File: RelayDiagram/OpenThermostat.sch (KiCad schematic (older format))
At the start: 18 parts, among them J2 Conn_01x15_Female, J3 Conn_01x15_Female

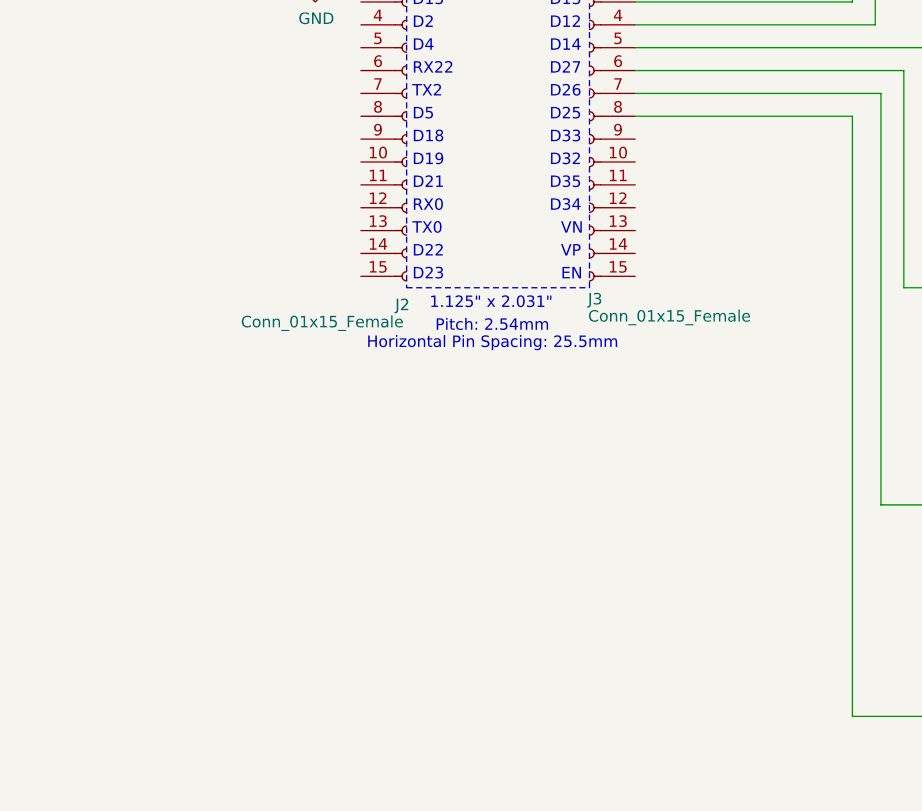
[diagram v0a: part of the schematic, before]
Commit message: Added LCD to full schematic, Changed LCD Symbol
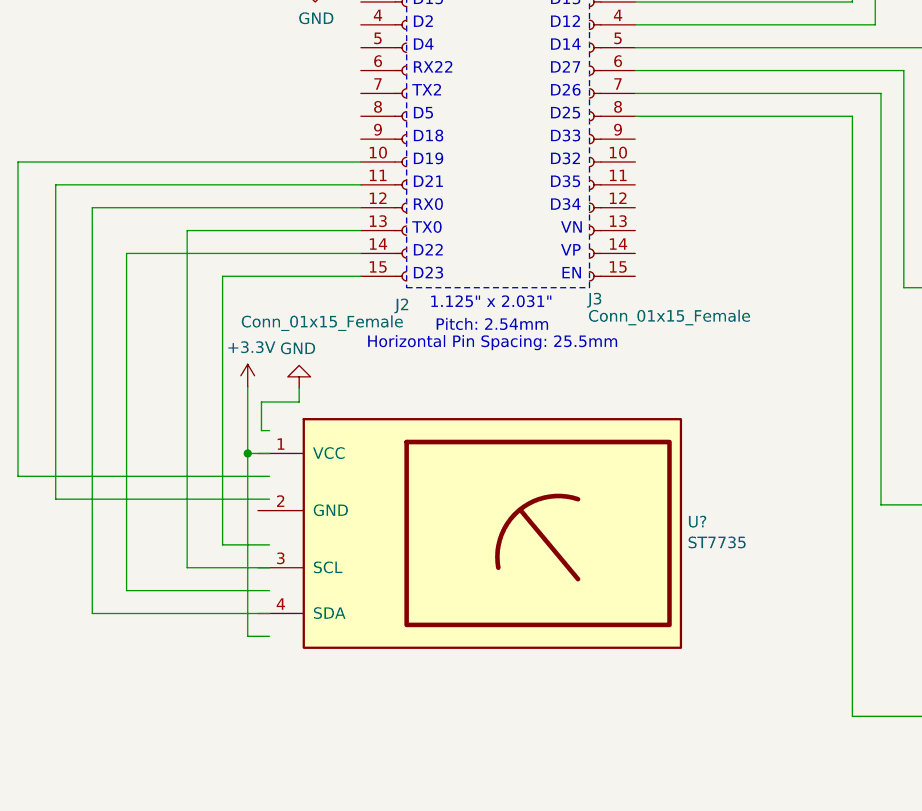
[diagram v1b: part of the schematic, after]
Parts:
- added U?: ST7735, symbol SeniorDesignLibrary:ST7735
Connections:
- net labels added: +3.3V
- wire segments 109 -> 135
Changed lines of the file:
@@
 Wire Wire Line
 	7700 1425 7750 1425
+$Comp
+L SeniorDesignLibrary:ST7735 U?
+U 1 1 5C414B96
+P 2900 5200
+F 0 "U?" H 4179 5200 50  0000 L CNN
+F 1 "ST7735" H 4179 5109 50  0000 L CNN
+F 2 "" H 2900 5200 50  0001 C CNN
+F 3 "" H 2900 5200 50  0001 C CNN
+	1    2900 5200
+	1    0    0    -1
+$EndComp
+Wire Wire Line
+	2750 4025 1725 4025
+Wire Wire Line
+	1725 4025 1725 5500
+Wire Wire Line
+	1725 5500 2350 5500
+Wire Wire Line
+	2350 5400 1990 5400
+Wire Wire Line
+	1990 5400 1990 3925
+Wire Wire Line
+	1990 3925 2750 3925
+Wire Wire Line
+	2350 5600 1575 5600
+Wire Wire Line
+	1575 5600 1575 3825
+Wire Wire Line
+	1575 3825 2750 3825
+Wire Wire Line
+	2350 5300 2145 5300
+Wire Wire Line
+	2145 5300 2145 4125
+Wire Wire Line
+	2145 4125 2750 4125
+$Comp
+L power:+3.3V #PWR?
+U 1 1 5C424F6C
+P 2255 4610
+F 0 "#PWR?" H 2255 4460 50  0001 C CNN
+F 1 "+3.3V" H 2270 4783 50  0000 C CNN
+F 2 "" H 2255 4610 50  0001 C CNN
+F 3 "" H 2255 4610 50  0001 C CNN
+	1    2255 4610
+	1    0    0    -1
+$EndComp
+$Comp
+L power:GND #PWR?
+U 1 1 5C42501F
+P 2480 4615
+F 0 "#PWR?" H 2480 4365 50  0001 C CNN
+F 1 "GND" H 2485 4442 50  0000 C CNN
+F 2 "" H 2480 4615 50  0001 C CNN
+F 3 "" H 2480 4615 50  0001 C CNN
+	1    2480 4615
+	-1   0    0    1
+$EndComp
+Wire Wire Line
+	2480 4675 2480 4615
+Wire Wire Line
+	2350 4900 2255 4900
+Wire Wire Line
+	2255 4900 2255 4610
+Wire Wire Line
+	2350 4800 2315 4800
+Wire Wire Line
+	2315 4800 2315 4675
+Wire Wire Line
+	2315 4675 2480 4675
+Wire Wire Line
+	2255 5700 2255 4900
+Wire Wire Line
+	2255 5700 2350 5700
+Connection ~ 2255 4900
+Wire Wire Line
+	2350 5100 1415 5100
+Wire Wire Line
+	1415 5100 1415 3725
+Wire Wire Line
+	1415 3725 2750 3725
+Wire Wire Line
+	2350 5000 1250 5000
+Wire Wire Line
+	1250 5000 1250 3625
+Wire Wire Line
+	1250 3625 2750 3625
 $EndSCHEMATC

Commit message: Some updates to the relay system for flyback and pulldown for FETs
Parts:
- added D? (x6): D, symbol Device:D
- added R? (x6): 100, symbol Device:R
- added R? (x6): 10k, symbol Device:R
- U?: symbol SeniorDesignLibrary:ST7735 -> OpenThermostat-rescue:ST7735-SeniorDesignLibrary
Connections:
- wire segments 135 -> 153

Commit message: added io for buttons and header for open pins, IO expander may not be needed because we have six open pins
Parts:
- removed D? (x6): D, symbol Device:D
- removed R? (x6): 100, symbol Device:R
- removed R? (x6): 10k, symbol Device:R
- added J?: Conn_01x06_Female, symbol Connector:Conn_01x06_Female
- added SW? (x6): SW_Push, symbol Switch:SW_Push
- U?: symbol OpenThermostat-rescue:ST7735-SeniorDesignLibrary -> SeniorDesignLibrary:ST7735
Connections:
- wire segments 153 -> 165

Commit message: added io expander, may need different pin for scl
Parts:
- removed J?: Conn_01x06_Female, symbol Connector:Conn_01x06_Female
- added J?: Conn_01x12_Female, symbol Connector:Conn_01x12_Female
- added R? (x3): 10k, symbol Device:R
- added U?: PCF8574, symbol Interface_Expansion:PCF8574
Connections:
- wire segments 165 -> 227

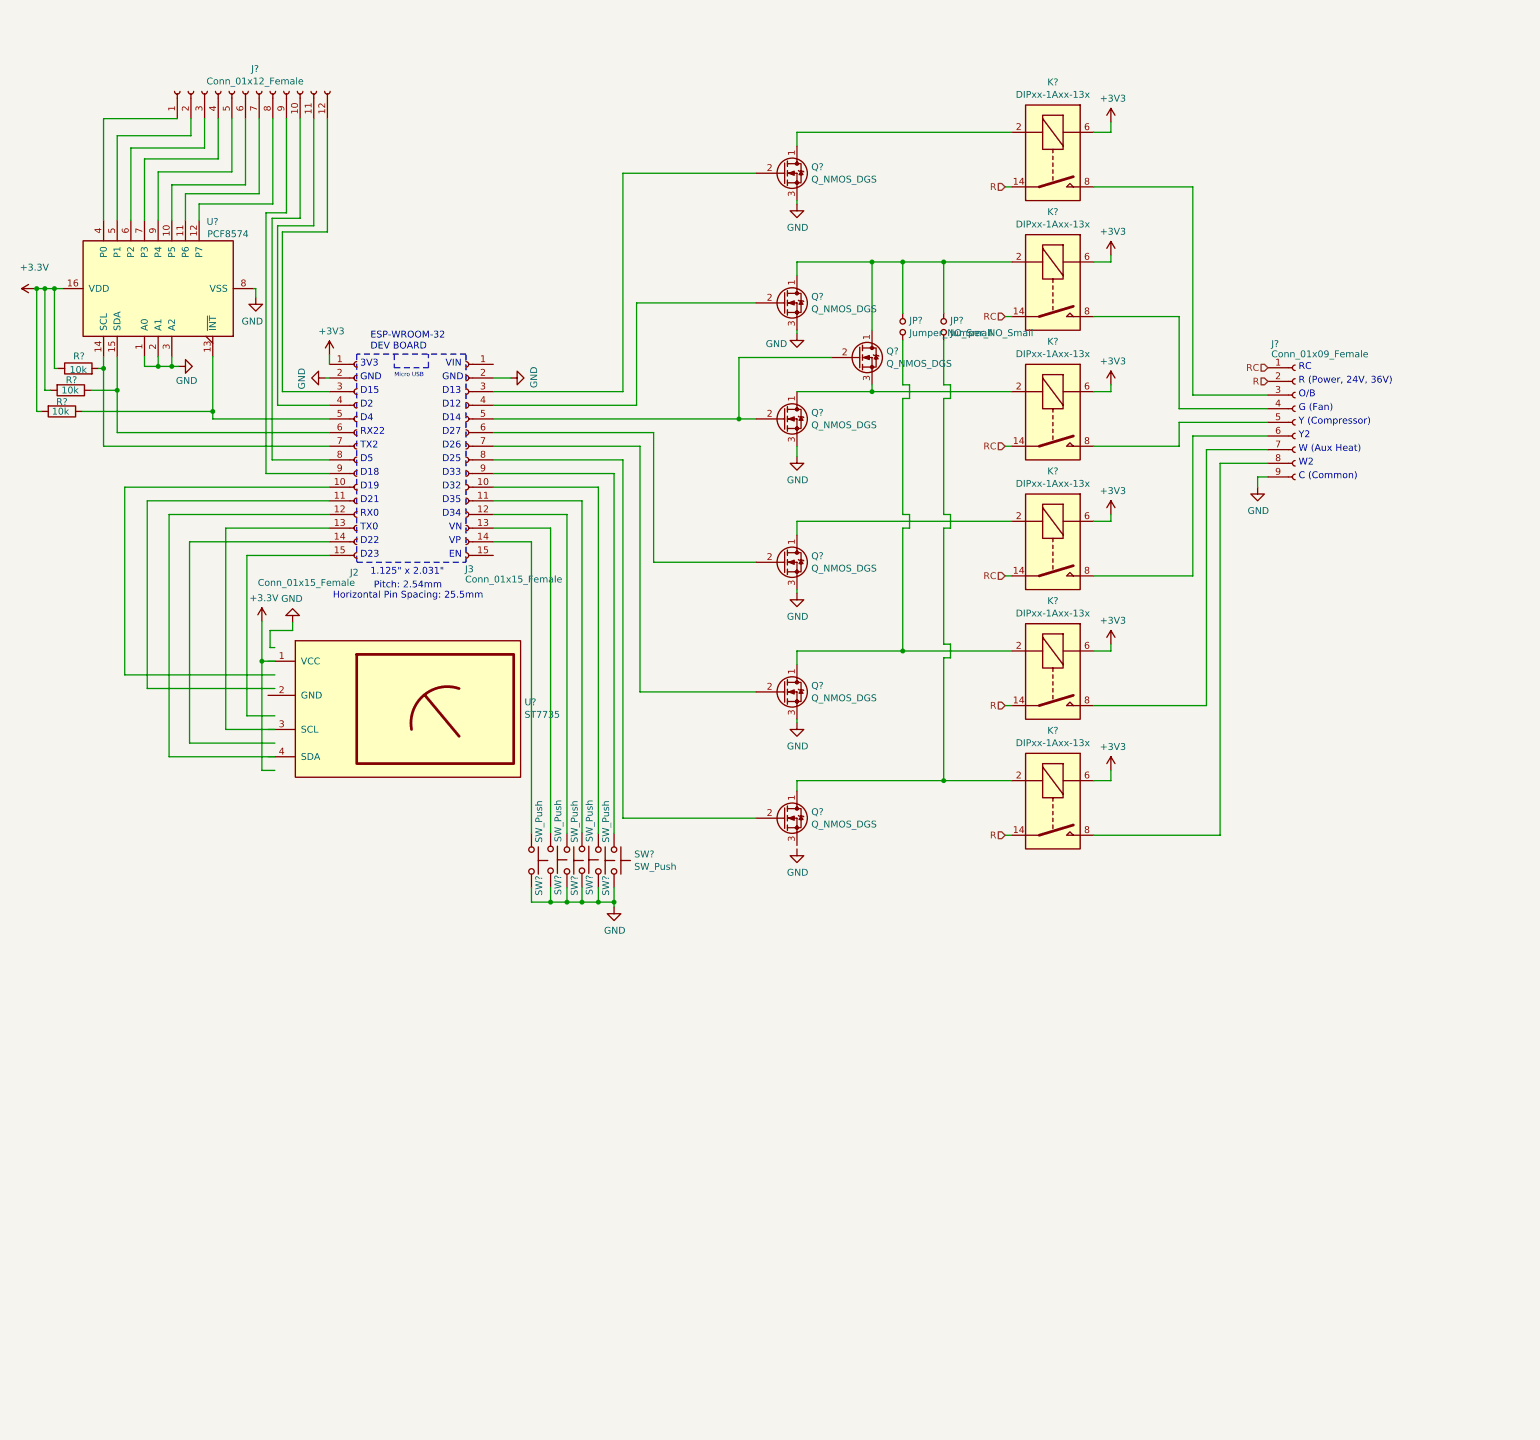
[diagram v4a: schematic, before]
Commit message: Fixed My mistake overwriting the relay protection
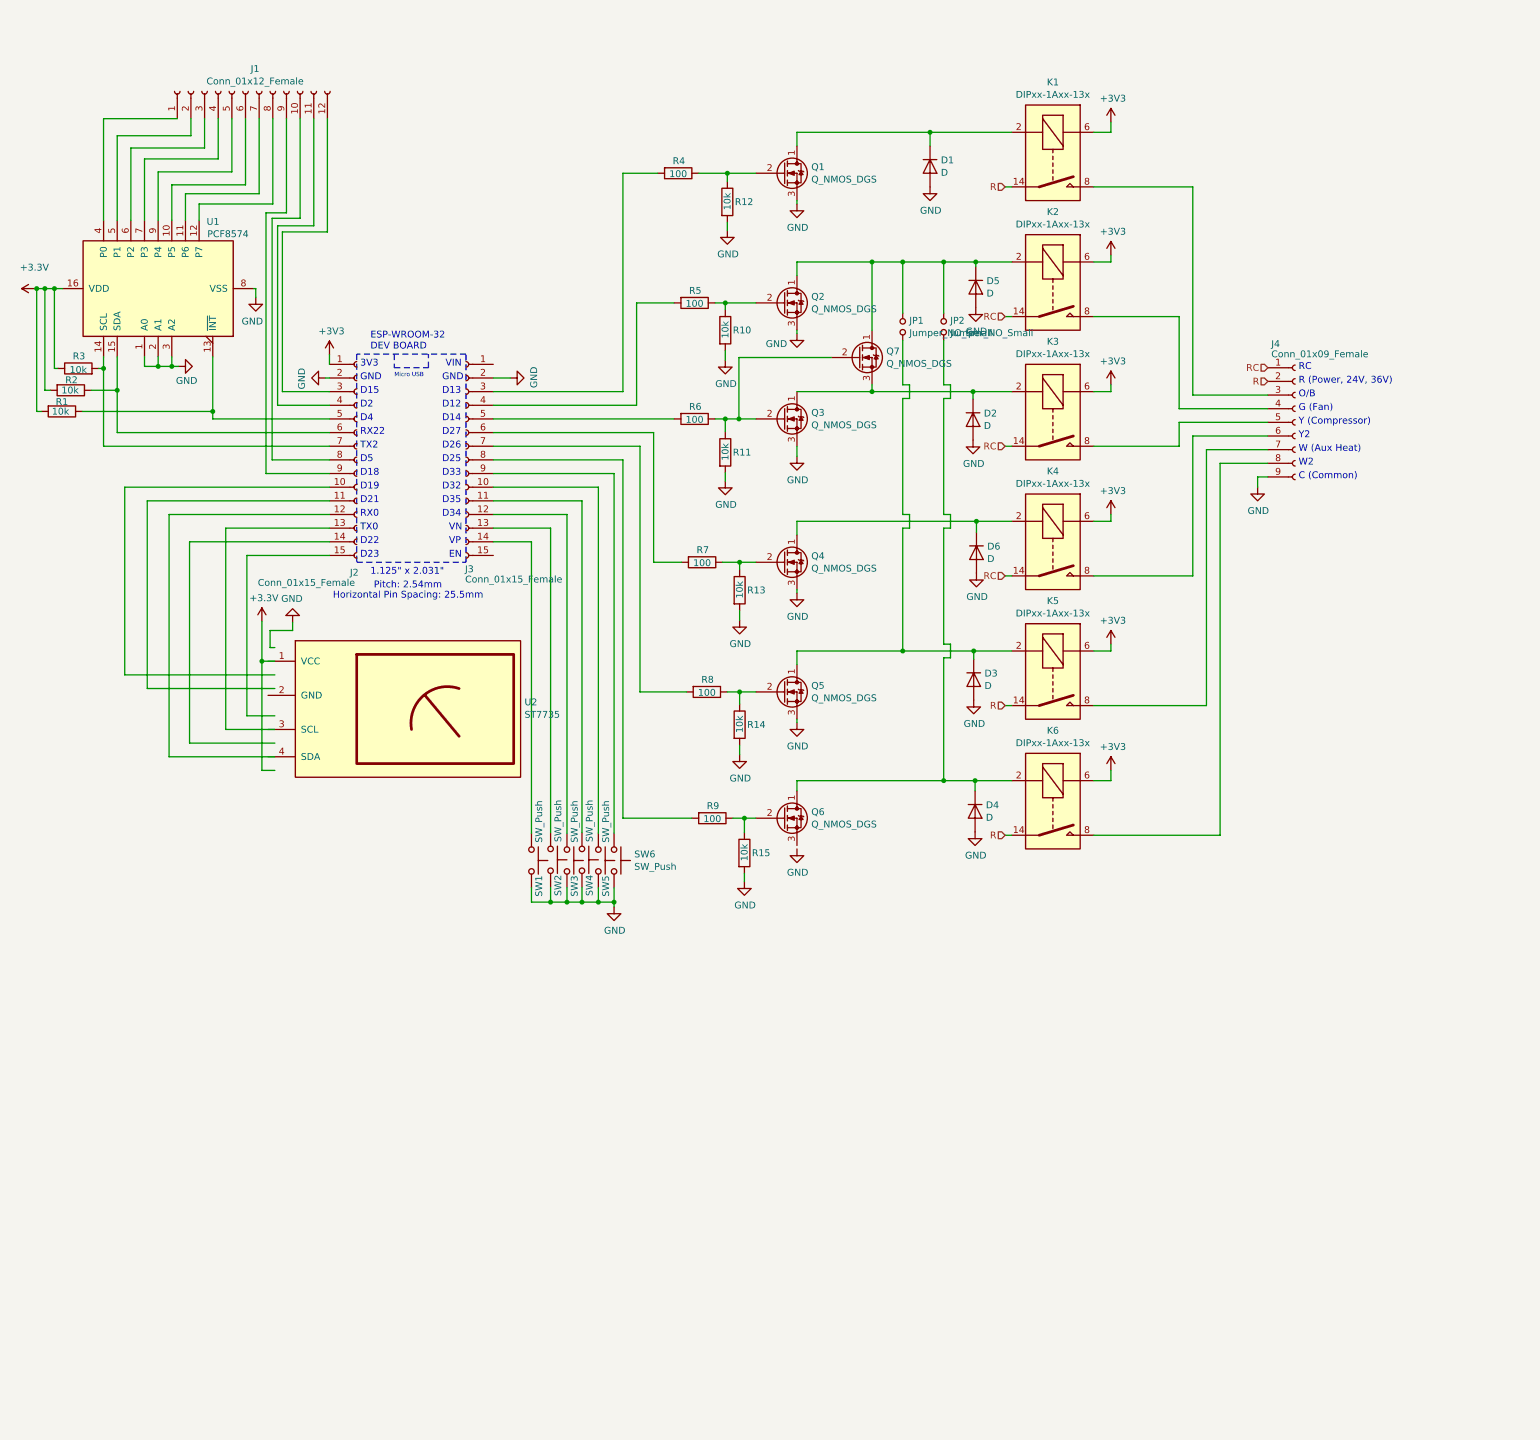
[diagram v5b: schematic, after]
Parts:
- added D1, D2, D3, D4, D5, D6: D, symbol Device:D
- added R10, R11, R12, R13, R14, R15: 10k, symbol Device:R
- added R4, R5, R6, R7, R8, R9: 100, symbol Device:R
- gave numbers to parts that had none: 28
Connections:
- wire segments 227 -> 263

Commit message: Comments
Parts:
- U2: symbol SeniorDesignLibrary:ST7735 -> OpenThermostat-rescue:ST7735-SeniorDesignLibrary
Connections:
- wire segments 263 -> 259
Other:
- note added: "Replace with SD1306?"
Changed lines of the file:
@@
 $EndComp
-Wire Wire Line
-	6175 4825 6950 4825
 Wire Wire Line
 	6950 2550 6950 2875
@@
 Wire Wire Line
 	6950 3825 7000 3825
-Connection ~ 6950 4825
-Wire Wire Line
-	6175 5775 7250 5775
 Wire Wire Line
 	7250 3825 7300 3825
@@
 	7300 4875 7250 4875
 Wire Wire Line
-	7250 4875 7250 5775
-Connection ~ 7250 5775
-Wire Wire Line
 	6950 3925 7000 3925
 Wire Wire Line
 	7000 3925 7000 3825
-Wire Wire Line
-	6950 3925 6950 4825
 Wire Wire Line
 	7250 3825 7250 2975
@@
 	7700 1425 7750 1425
 $Comp
-L SeniorDesignLibrary:ST7735 U2
+L OpenThermostat-rescue:ST7735-SeniorDesignLibrary U2
 U 1 1 5C414B96
 P 2900 5200
@@
 Wire Wire Line
 	7480 5850 7480 5775
-Wire Wire Line
-	7250 5775 7480 5775
 Connection ~ 7480 5775
 Wire Wire Line
@@
 Wire Wire Line
 	7470 4885 7470 4825
-Wire Wire Line
-	6950 4825 7470 4825
 Connection ~ 7470 4825
 Wire Wire Line
@@
 	1    0    0    -1
 $EndComp
+Text Notes 2500 5875 0    50   ~ 0
+Replace with SD1306?
+Wire Wire Line
+	6175 4825 7470 4825
+Wire Wire Line
+	6175 5775 7480 5775
 $EndSCHEMATC

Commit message: Swapped out LCD and Rearranged pins to better implement I2C and the new relays
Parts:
- removed J1: Conn_01x12_Female, symbol Connector:Conn_01x12_Female
- removed SW1: SW_Push, symbol Switch:SW_Push
- removed U2: ST7735, symbol OpenThermostat-rescue:ST7735-SeniorDesignLibrary
- added J?: Conn_01x10_Female, symbol Connector:Conn_01x10_Female
- added R?: 5k, symbol Device:R
- added U?: ST7735, symbol SeniorDesignLibrary:ST7735
- added U?: DHT11, symbol Sensor:DHT11
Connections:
- wire segments 259 -> 252
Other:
- note removed: "Replace with SD1306?"
- moved on the sheet: SW2, SW3, SW4, SW5, SW6

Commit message: Double coil latching relays
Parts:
- removed D1, D2, D3, D4, D5, D6: D, symbol Device:D
- removed J4: Conn_01x09_Female, symbol Connector:Conn_01x09_Female
- removed J?: Conn_01x10_Female, symbol Connector:Conn_01x10_Female
- removed JP1, JP2: Jumper_NO_Small, symbol Device:Jumper_NO_Small
- removed K1, K2, K3, K4, K5, K6: DIPxx-1Axx-13x, Relay_THT:Relay_StandexMeder_DIP_LowProfile, symbol Relay:DIPxx-1Axx-13x
- removed Q1, Q2, Q3, Q4, Q5, Q6, Q7: Q_NMOS_DGS, symbol Device:Q_NMOS_DGS
- removed R10, R11, R12, R13, R14, R15: 10k, symbol Device:R
- removed R4, R5, R6, R7, R8, R9: 100, symbol Device:R
- added D? (x12): D, symbol Device:D
- added J?: Conn_01x09_Female, symbol Connector:Conn_01x09_Female
- added J?: Conn_01x08_Female, symbol Connector:Conn_01x08_Female
- added Q? (x12): Q_NMOS_DGS, symbol Device:Q_NMOS_DGS
- added R? (x12): 100, symbol Device:R
- added R? (x12): 1M, symbol Device:R
- added U? (x6): EE2-3TNU-L_DPDT_Relay, symbol SeniorDesignLibrary:EE2-3TNU-L_DPDT_Relay
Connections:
- wire segments 252 -> 299
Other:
- note added: "G (FAN)"
